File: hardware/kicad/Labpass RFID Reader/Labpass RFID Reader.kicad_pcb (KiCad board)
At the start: 2 copper layers, 74 x 74 mm, 59 parts, among them J1 Conn_01x03_Male, J2 Conn_01x08, J3 Conn_01x02, Q1 BC517, U1 adafruit_huzzah_32, U2 LM393, U3 LM324, U4 MFRC522, Y1 27.12 MHz

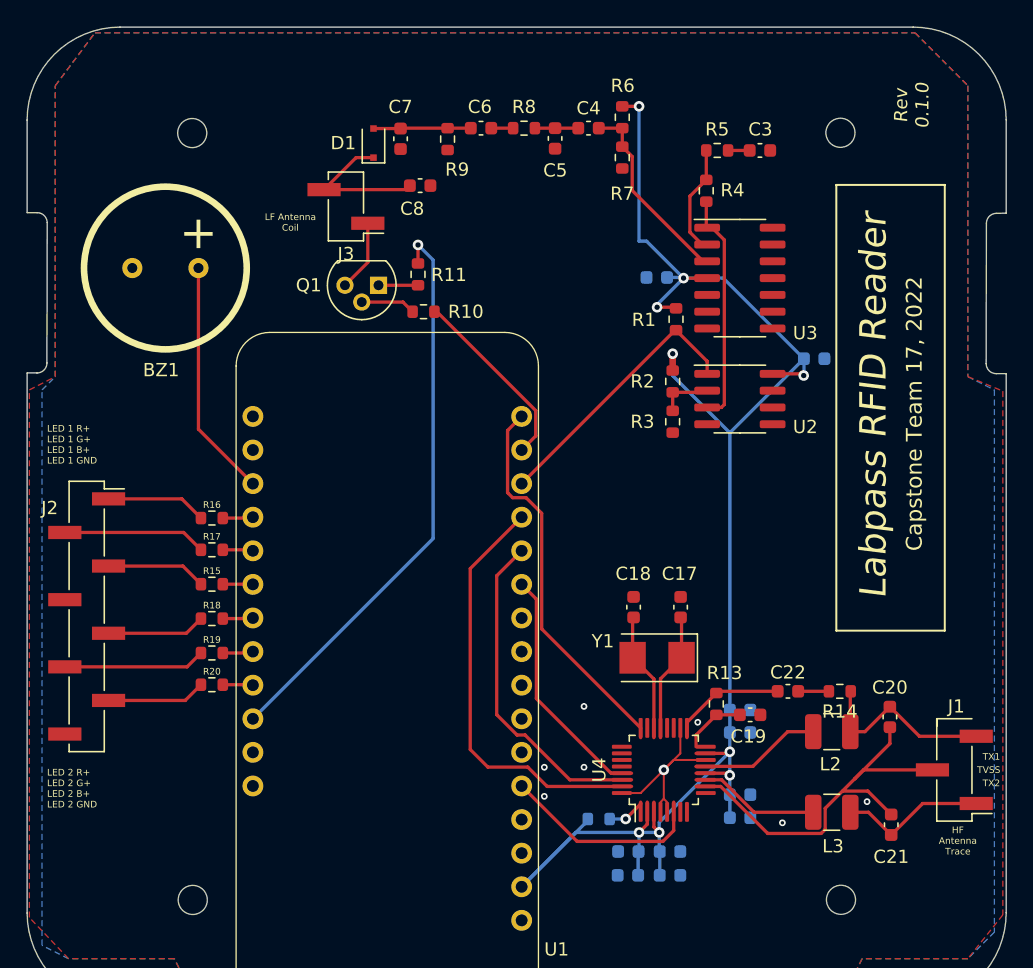
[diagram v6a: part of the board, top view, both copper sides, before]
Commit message: Several fixes
* EA and I2C were backwards
* Adding missing Crx into HF receive path
* Better header size and placement
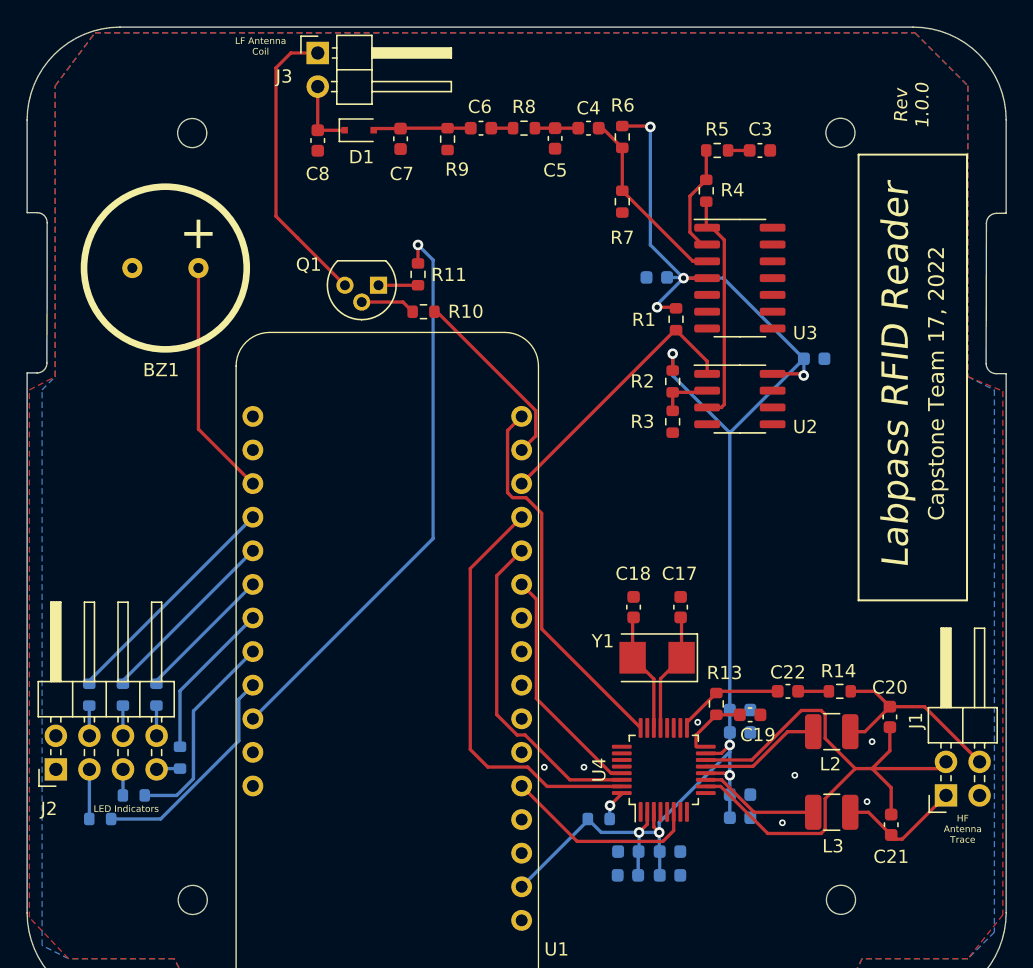
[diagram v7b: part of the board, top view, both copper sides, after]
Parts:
- J1: footprint Connector_PinHeader_2.54mm:PinHeader_1x03_P2.54mm_Vertical_SMD_Pin1Left -> Connector_PinHeader_2.54mm:PinHeader_2x02_P2.54mm_Horizontal
- J2: footprint Connector_PinHeader_2.54mm:PinHeader_1x08_P2.54mm_Vertical_SMD_Pin1Right -> Connector_PinHeader_2.54mm:PinHeader_2x04_P2.54mm_Horizontal
- J3: footprint Connector_PinHeader_2.54mm:PinHeader_1x02_P2.54mm_Vertical_SMD_Pin1Left -> Connector_PinHeader_2.54mm:PinHeader_1x02_P2.54mm_Horizontal
- R15, R16, R17, R18, R19, R20: moved to B.Cu
- moved R16 16.3 mm to (111.0, 108.7), turned to -90 degrees
- moved R19 15.1 mm to (111.8, 118.1)
- moved R17 12.9 mm to (113.5, 108.7), turned to -90 degrees
- moved J3 11.8 mm to (128.3, 60.2), turned to 0 degrees
- moved J2 11.8 mm to (108.5, 114.4), turned to 90 degrees
- moved R18 10.8 mm to (117.9, 113.5), turned to -90 degrees
- moved R20 10.2 mm to (114.4, 116.3)
- moved R15 9.34 mm to (116.1, 108.7), turned to -90 degrees
- moved C8 8.46 mm to (128.3, 66.8), turned to -90 degrees
- moved R7 3.33 mm to (151.3, 71.4)
- moved J1 2.03 mm to (175.8, 116.3), turned to 90 degrees
- moved R6 1.49 mm to (151.3, 66.5)
- moved D1 1.45 mm to (131.4, 66.0), turned to 0 degrees
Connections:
- J1 pad 3: Net-(R14-Pad1) -> unconnected-(J1-Pad3)
- J2 pad 1: Net-(J2-Pad1) -> GND
- J2 pad 2: Net-(J2-Pad2) -> GND
- J2 pad 4: GND -> Net-(J2-Pad4)
- J2 pad 8: GND -> Net-(J2-Pad8)
- R15 pad 2: Net-(J2-Pad3) -> Net-(J2-Pad8)
- R16 pad 2: Net-(J2-Pad1) -> Net-(J2-Pad4)
- R17 pad 2: Net-(J2-Pad2) -> Net-(J2-Pad6)
- R18 pad 2: Net-(J2-Pad5) -> Net-(J2-Pad7)
- R19 pad 1: /Indicators/LED_2_G -> /Indicators/LED_2_B
- R19 pad 2: Net-(J2-Pad6) -> Net-(J2-Pad3)
- R20 pad 1: /Indicators/LED_2_B -> /Indicators/LED_2_G
- R20 pad 2: Net-(J2-Pad7) -> Net-(J2-Pad5)
- U4 pad 1: Net-(R12-Pad2) -> GND
- U4 pad 14: GND -> /labpass_rf_13.56M/TVSS
- U4 pad 32: GND -> Net-(R12-Pad2)
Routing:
- net Net-(J3-Pad1): track 5.41 -> 22.2 mm
- net /Indicators/LED_1_R: track 2.30 -> 17.7 mm
- net /labpass_rf_13.56M/TVSS: track 31.7 -> 46.7 mm
- net /Indicators/LED_2_B: track 2.29 -> 16.7 mm
- net /Indicators/LED_2_G: track 2.32 -> 15.7 mm
- net /Indicators/LED_1_G: track 2.31 -> 14.1 mm
- net GND: track 11.8 -> 0.00 mm, vias 8 -> 7
- net Net-(J2-Pad2): track 10.8 -> 0.00 mm
- net +3V3: track 129.3 -> 118.9 mm
- net /Indicators/LED_2_R: track 2.29 -> 12.0 mm
- net Net-(J2-Pad6): track 10.7 -> 2.29 mm
- net /Indicators/LED_1_B: track 2.28 -> 10.5 mm
- net Net-(J2-Pad1): track 7.59 -> 0.00 mm
- net Net-(C8-Pad1): track 11.4 -> 5.33 mm
- net Net-(J2-Pad7): track 7.48 -> 1.79 mm
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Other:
- board text added: "LED Indicators"
- board text added: "Rev 1.0.0"
- board text removed: "LED 1 R+ LED 1 G+ LED 1 B+ LED 1 GND"
- board text removed: "LED 2 R+ LED 2 G+ LED 2 B+ LED 2 GND"
- board text removed: "Rev 0.1.0"
- board text removed: "TVSS"
- board text removed: "TX1"
- board text removed: "TX2"

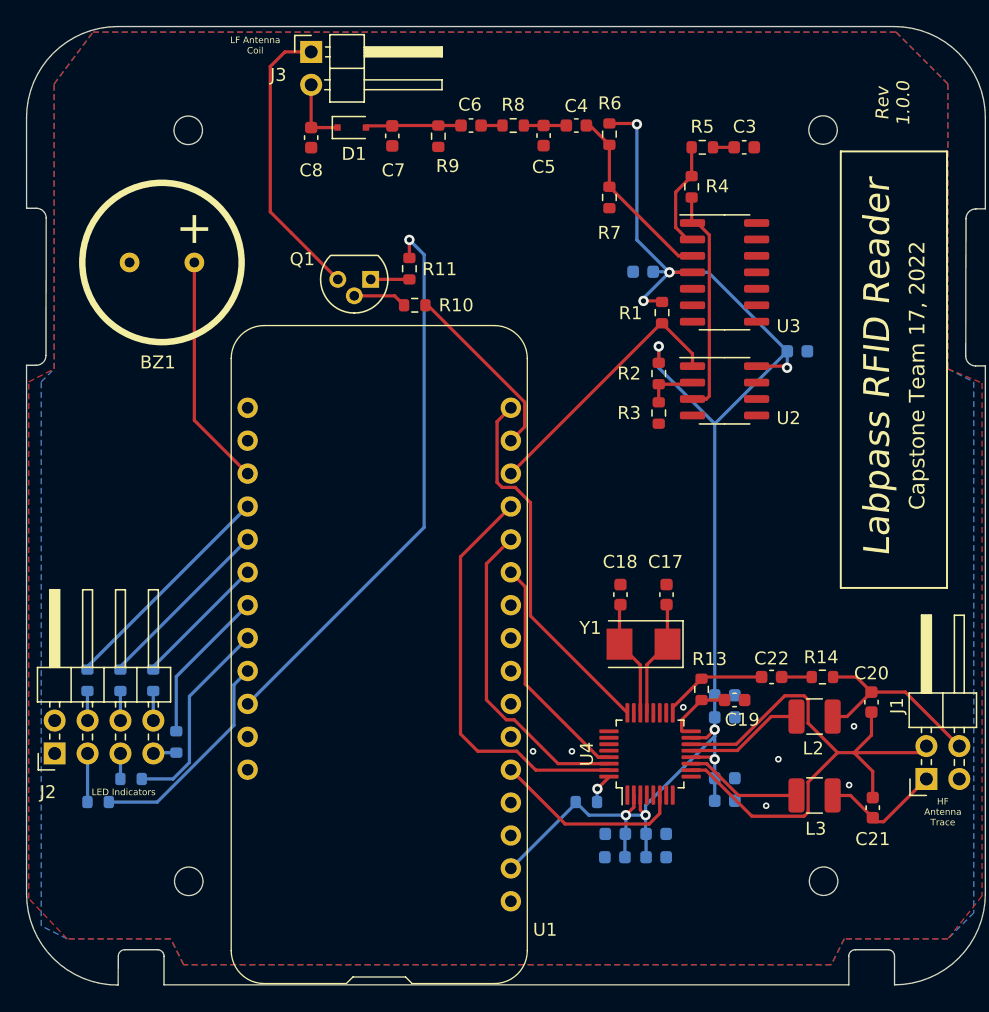
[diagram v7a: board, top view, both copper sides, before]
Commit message: Additional Changes
* remove transistor on LF path and power coil directly
  from ESP TX pin at 3.3V
* add some test points around the HF path
* add some cheap pots on LF for tuning the amplifier bias
  and comparator threshold
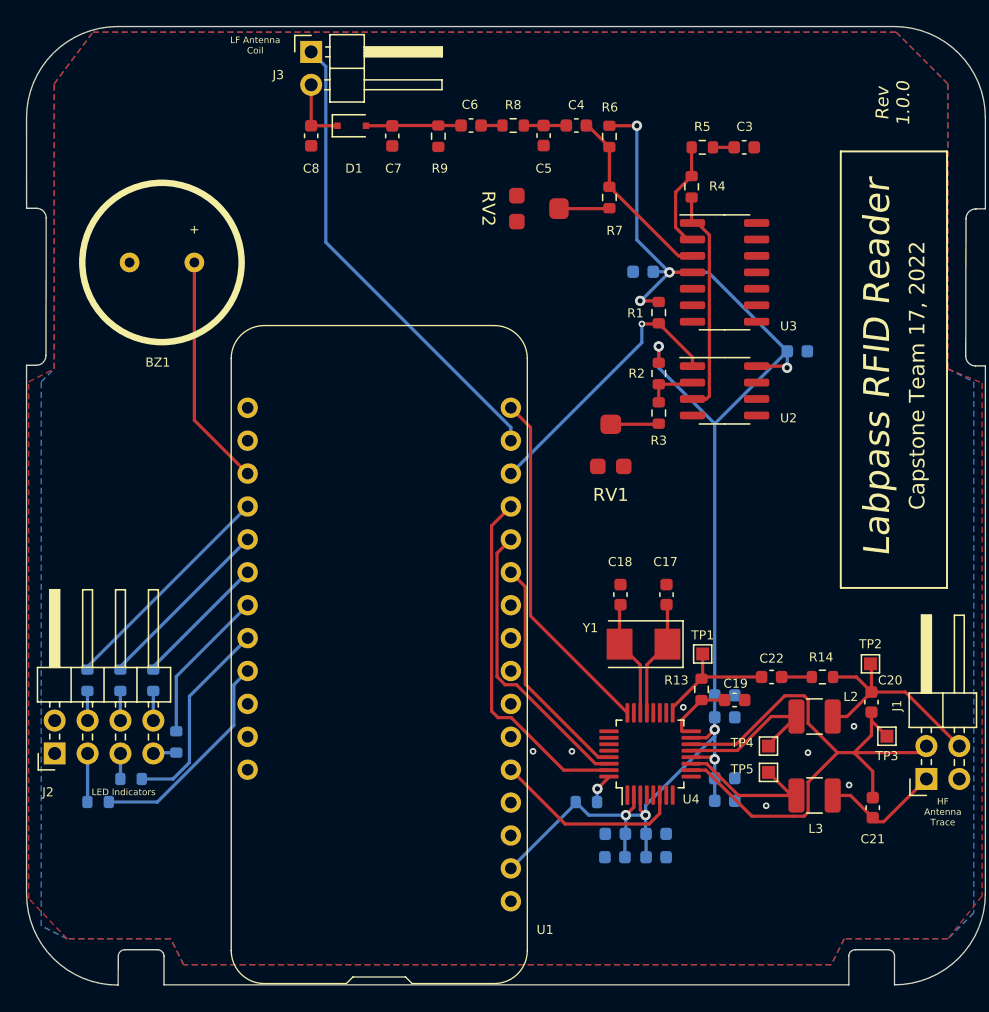
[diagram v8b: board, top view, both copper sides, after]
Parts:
- removed Q1: BC517, Package_TO_SOT_THT:TO-92
- removed R10: 1k, Resistor_SMD:R_0603_1608Metric
- removed R11: 56, Resistor_SMD:R_0603_1608Metric
- removed REF** (x4): MountingHole_2.2mm_M2_ISO14580, MountingHole:MountingHole_2.2mm_M2_ISO14580
- added RV1: 50k, Capstone Footprint Library:TC33X, F.Cu at (151.4, 90.4)
- added RV2: 50k, Capstone Footprint Library:TC33X, F.Cu at (145.9, 72.3)
- added TP1: TestPoint, TestPoint:TestPoint_Pad_1.0x1.0mm, F.Cu at (158.5, 106.7)
- added TP2: TestPoint, TestPoint:TestPoint_Pad_1.0x1.0mm, F.Cu at (171.4, 107.4)
- added TP3: TestPoint, TestPoint:TestPoint_Pad_1.0x1.0mm, F.Cu at (172.7, 113.0)
- added TP4: TestPoint, TestPoint:TestPoint_Pad_1.0x1.0mm, F.Cu at (163.6, 113.8)
- added TP5: TestPoint, TestPoint:TestPoint_Pad_1.0x1.0mm, F.Cu at (163.6, 115.8)
- R2: value 330k -> 220k
- R3: value 110k -> 47k
- R7: value 100k -> 82k
- moved R1 0.26 mm to (155.1, 80.3)
- moved R6 0.18 mm to (151.3, 66.7)
- moved C8 0.14 mm to (128.3, 66.7)
- moved D1 0.14 mm to (131.4, 65.9)
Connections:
- J3 pad 1: Net-(J3-Pad1) -> /labpass_rf_125k/LF_RF_TX
- R3 pad 2: GND -> Net-(R3-Pad2)
- R7 pad 2: GND -> Net-(R7-Pad2)
- U1 pad BAT: (no net) -> unconnected-(U1-PadBAT)
- U1 pad EN: (no net) -> unconnected-(U1-PadEN)
- U1 pad NC: (no net) -> unconnected-(U1-PadNC)
- U1 pad RST: (no net) -> unconnected-(U1-PadRST)
- U1 pad USB: +5V -> Net-(U1-PadUSB)
- U2 pad 5: (no net) -> unconnected-(U2-Pad5)
- U2 pad 6: (no net) -> unconnected-(U2-Pad6)
- U2 pad 7: (no net) -> unconnected-(U2-Pad7)
- U3 pad 10: (no net) -> unconnected-(U3-Pad10)
- U3 pad 12: (no net) -> unconnected-(U3-Pad12)
- U3 pad 13: (no net) -> unconnected-(U3-Pad13)
- U3 pad 14: (no net) -> unconnected-(U3-Pad14)
- U3 pad 5: (no net) -> unconnected-(U3-Pad5)
- U3 pad 6: (no net) -> unconnected-(U3-Pad6)
- U3 pad 7: (no net) -> unconnected-(U3-Pad7)
- U3 pad 8: (no net) -> unconnected-(U3-Pad8)
- U3 pad 9: (no net) -> unconnected-(U3-Pad9)
- U4 pad 19: (no net) -> unconnected-(U4-Pad19)
- U4 pad 20: (no net) -> unconnected-(U4-Pad20)
- U4 pad 23: (no net) -> unconnected-(U4-Pad23)
- U4 pad 25: (no net) -> unconnected-(U4-Pad25)
- U4 pad 26: (no net) -> unconnected-(U4-Pad26)
- U4 pad 27: (no net) -> unconnected-(U4-Pad27)
- U4 pad 28: (no net) -> unconnected-(U4-Pad28)
- U4 pad 7: (no net) -> unconnected-(U4-Pad7)
- U4 pad 8: (no net) -> unconnected-(U4-Pad8)
- U4 pad 9: (no net) -> unconnected-(U4-Pad9)
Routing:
- net +5V: track 43.3 -> 0.00 mm, vias 1 -> 0
- net /labpass_rf_125k/LF_RF_TX: track 14.2 -> 36.4 mm
- net Net-(J3-Pad1): track 22.2 -> 0.00 mm
- net /labpass_rf_13.56M/MISO: track 31.8 -> 27.4 mm
- net Net-(Q1-Pad2): track 4.15 -> 0.00 mm
- net Net-(R7-Pad2): track 0.00 -> 3.86 mm
- net Net-(R3-Pad2): track 0.00 -> 3.72 mm
- net /labpass_rf_13.56M/TX2: track 9.22 -> 12.4 mm
- net Net-(Q1-Pad1): track 2.98 -> 0.00 mm
- net /labpass_rf_13.56M/TX1: track 9.14 -> 12.0 mm
- net /labpass_rf_13.56M/TVSS: track 46.7 -> 49.1 mm
- net Net-(C20-Pad2): track 15.7 -> 17.9 mm
- net /labpass_rf_13.56M/MOSI: track 24.7 -> 22.5 mm
- net /labpass_rf_13.56M/RX: track 7.83 -> 9.78 mm
- net /labpass_rf_13.56M/SDA: track 28.8 -> 27.3 mm
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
